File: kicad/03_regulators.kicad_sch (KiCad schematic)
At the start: 20 parts, among them U10 TPS73033DBVT, U3 TPS73033DBVT, U8 K7805-2000R3, U9 VXO7805-500

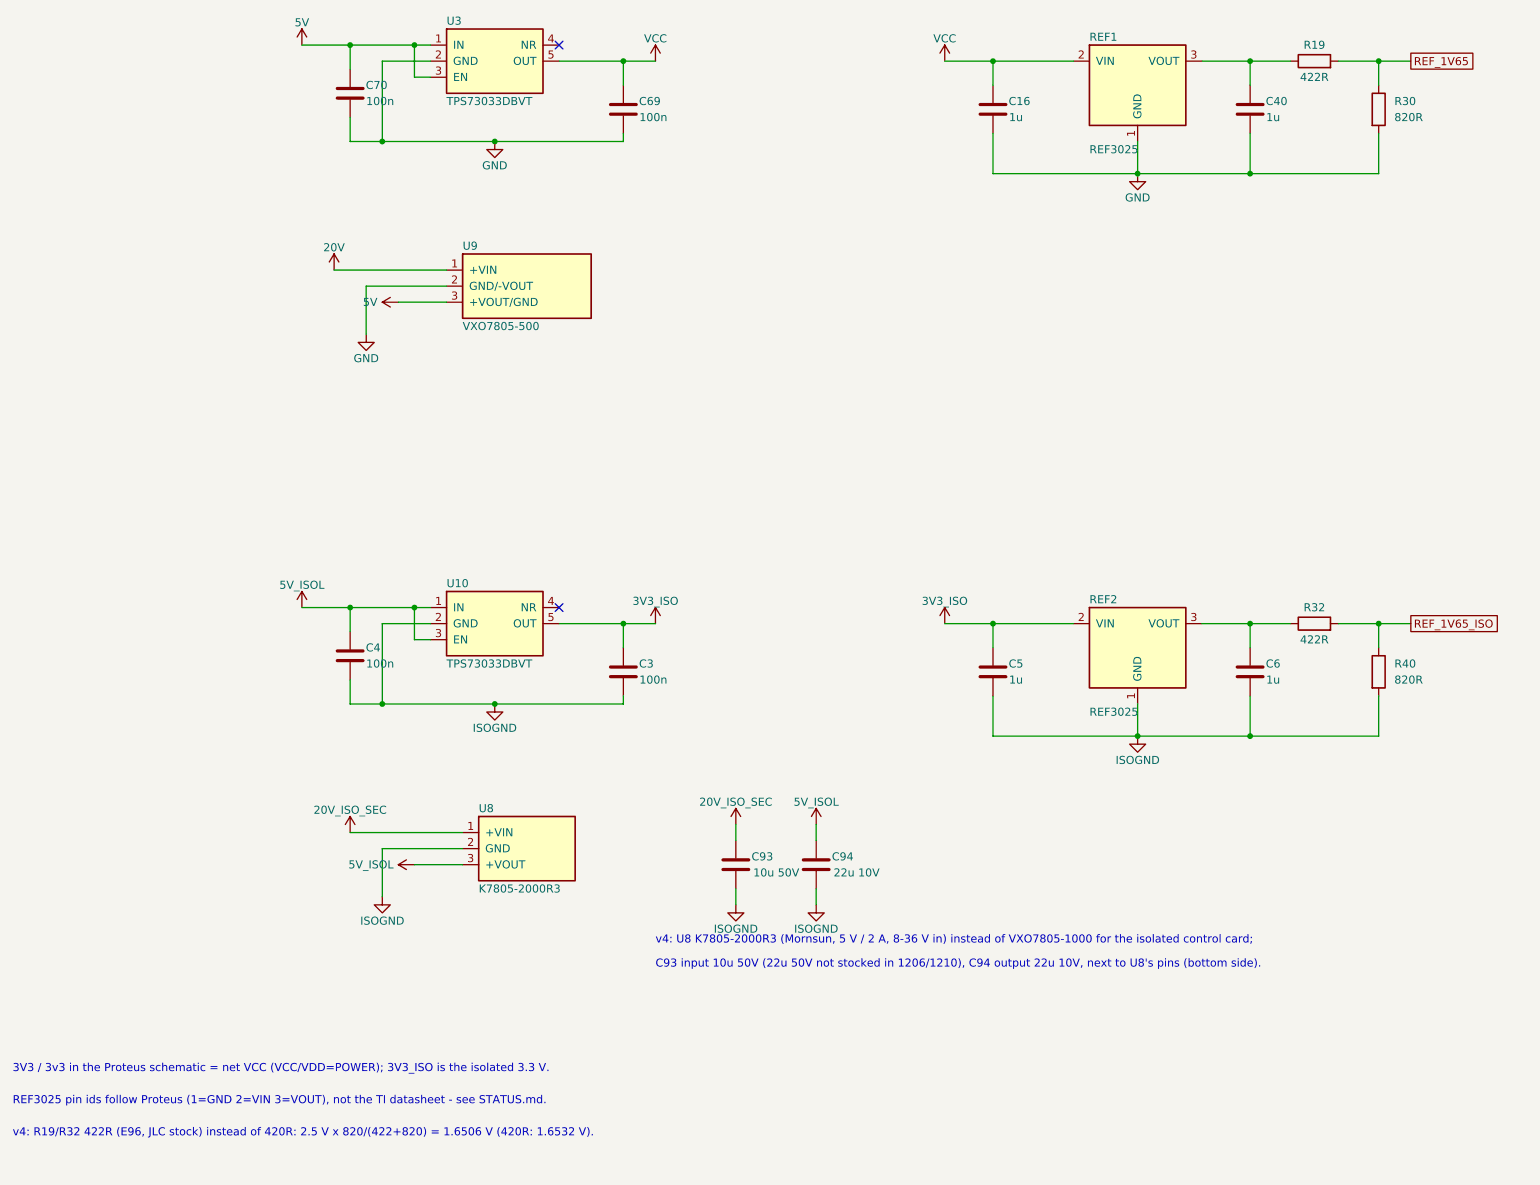
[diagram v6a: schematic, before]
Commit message: v4 fix 11/12: measurement filters (reports/noise findings 1-5), AMC1306M05
Schematic (sheets 1/3/4/5/9): C95-C106 1n C0G across every 10k leg of the six
difference amplifiers (15.9 kHz tap-node filter), R7 1k -> 10k (U1B + leg
matched; ADA3 scaling changes), R18/R9 100R -> 8.2k with C88/C89 4.7n C0G and
new C107/C108 4.7n on ISOADA1/2 (4.1 kHz), C42/C2 1n -> 10n C0G (1.9 kHz DC
links), C109/C110 100n on REF_1V65/REF_1V65_ISO. R64/DAB series R unchanged
(L unknown; 25R per leg for 10 nH).
Board: fix 11 places the 16 caps (10 top beside their resistor, 6 bottom with
7 vias), renames six auto-named output nets, sets the values; fix 12 re-runs
fix 8's silk placement. DRC 293 (+1 silk), 0 shorts/unconnected/parity.
Deviation rows, v4_copper vias/areas, part map. Replay of fixes 1-12 on the
tag's board gives the board and edit log.
fab: C0G codes C307441/C1518204/C22400107, U4-U6 AMC1306M05DWVR (C701717,
+-50 mV, 4.9k R_IND, checked in SBAS734D), CPL 205 parts, stock for 5 boards
(AMC1306M05: 5 in stock). Noise report: CMTI 50 kV/us min correction.

Co-Authored-By: Claude Opus 5.5 <noreply@anthropic.com>
Claude-Session: https://claude.ai/code/session_01Am5hpeWpvZbzmHWspFiWJm
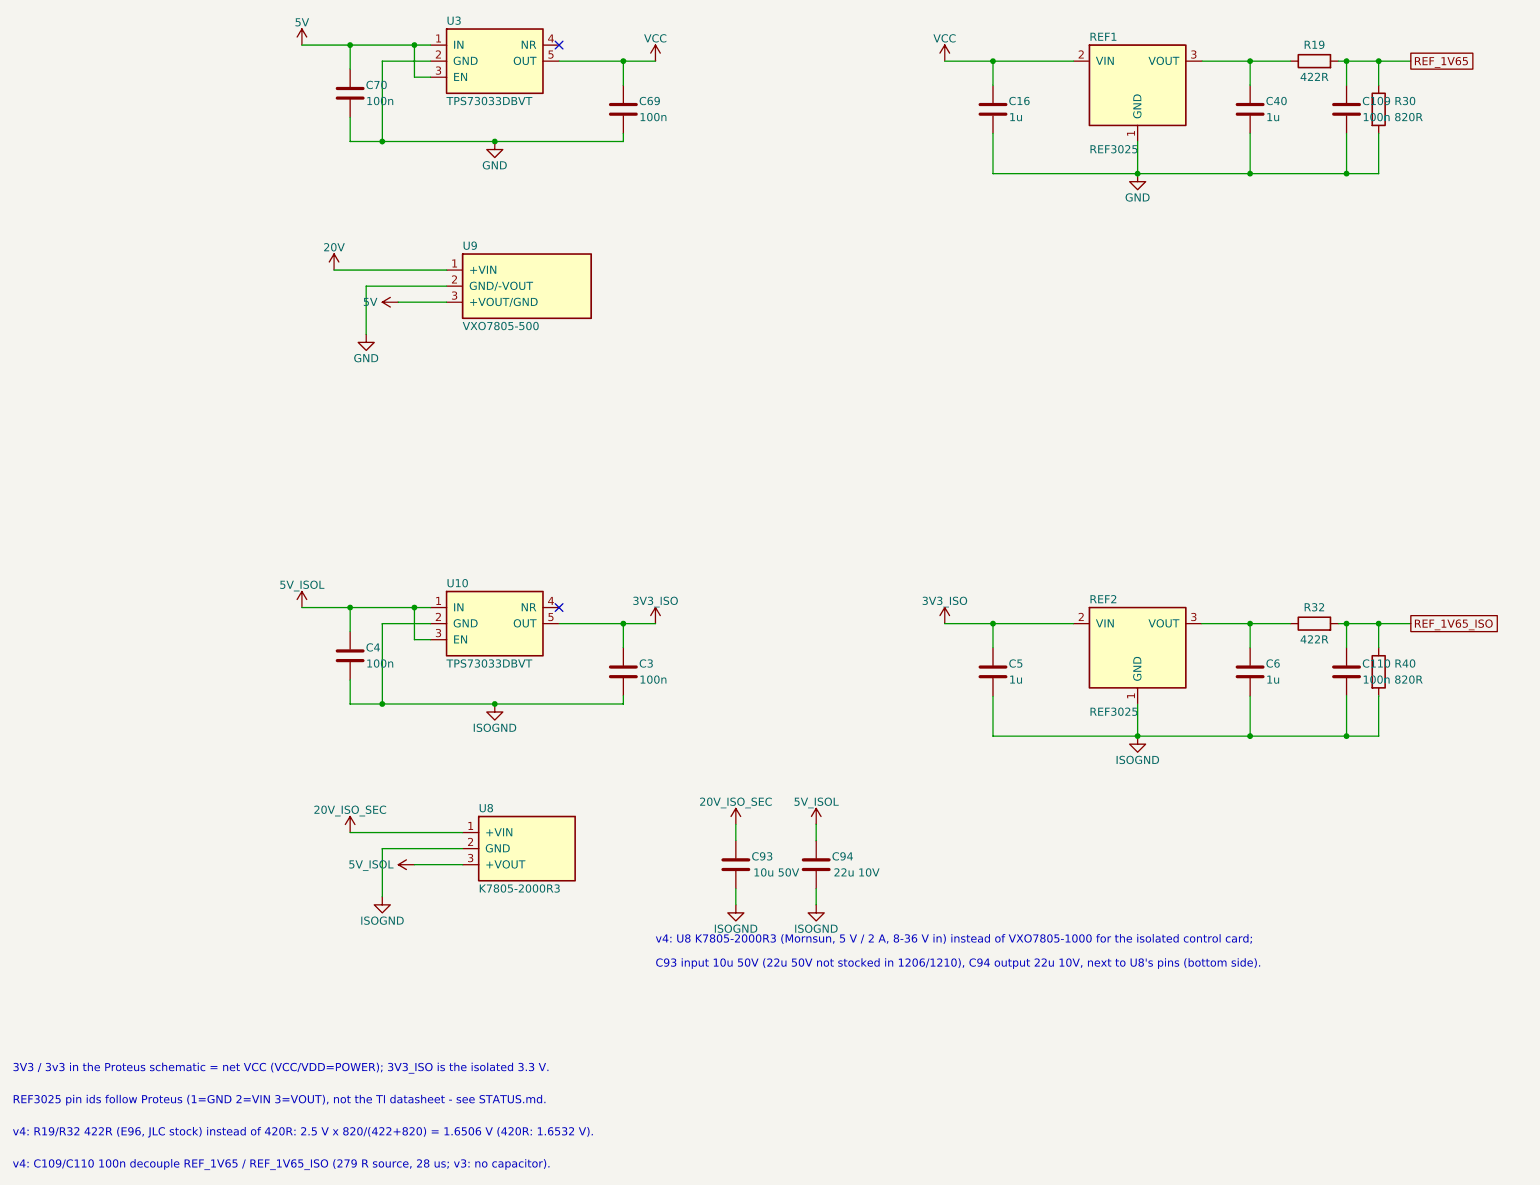
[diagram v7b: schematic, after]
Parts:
- added C109, C110: 100n, Capacitor_SMD:C_0402_1005Metric, symbol ac_psu:C
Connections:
- net GND: now also C109.2
- net ISOGND: now also C110.2
- net REF_1V65: now also C109.1
- net REF_1V65_ISO: now also C110.1
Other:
- note added: "v4: C109/C110 100n decouple REF_1V65 / REF_1V65_ISO (279 R source, 28 us; v3: no capacitor)."
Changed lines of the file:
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@@
+	)
+	(symbol
+		(lib_id "ac_psu:C")
+		(at 236.22 58.42 0)
+		(unit 1)
+		(exclude_from_sim no)
+		(in_bom yes)
+		(on_board yes)
+		(dnp no)
+		(property "Reference" "C109"
+			(at 240.96 57.15 0)
+			(effects
+				(font
+					(size 1.27 1.27)
+				)
+			)
+		)
+		(property "Value" "100n"
+			(at 240.96 59.69 0)
+			(effects
+				(font
+					(size 1.27 1.27)
+				)
+			)
+		)
+		(property "Footprint" "Capacitor_SMD:C_0402_1005Metric"
+			(at 237.1852 62.23 0)
+			(effects
+				(font
+					(size 1.27 1.27)
+				)
+				(hide yes)
+			)
+		)
+		(property "Datasheet" ""
+			(at 236.22 58.42 0)
+			(effects
+				(font
+					(size 1.27 1.27)
+				)
+				(hide yes)
+			)
+		)
+		(property "Description" "Unpolarized capacitor"
+			(at 236.22 58.42 0)
+			(effects
+				(font
+					(size 1.27 1.27)
+				)
+				(hide yes)
+			)
+		)
+		(pin "1"
+		)
+		(pin "2"
+		)
+		(instances
+			(project "ac_psu"
+				(path "/04fb09b4-531d-41de-805c-3ed4ed6dcfa8/25c5ca54-388f-4b9c-876e-19a6fbb99a35"
+					(reference "C109")
+					(unit 1)
+				)
+			)
+		)
+	)
+	(wire
+		(pts
+			(xy 236.22 54.61) (xy 236.22 50.8)
+		)
+		(stroke
+			(width 0)
+			(type default)
+		)
+	)
+	(junction
+		(at 236.22 50.8)
+		(diameter 0)
+		(color 0 0 0 0)
+	)
+	(wire
+		(pts
+			(xy 236.22 62.23) (xy 236.22 68.58)
+		)
+		(stroke
+			(width 0)
+			(type default)
+		)
+	)
+	(junction
+		(at 236.22 68.58)
+		(diameter 0)
+		(color 0 0 0 0)
 	)
 	(symbol
@@
 		(color 0 0 0 0)
 	)
+	(symbol
+		(lib_id "ac_psu:C")
+		(at 236.22 147.32 0)
+		(unit 1)
+		(exclude_from_sim no)
+		(in_bom yes)
+		(on_board yes)
+		(dnp no)
+		(property "Reference" "C110"
+			(at 240.96 146.05 0)
+			(effects
+				(font
+					(size 1.27 1.27)
+				)
+			)
+		)
+		(property "Value" "100n"
+			(at 240.96 148.59 0)
+			(effects
+				(font
+					(size 1.27 1.27)
+				)
+			)
+		)
+		(property "Footprint" "Capacitor_SMD:C_0402_1005Metric"
+			(at 237.1852 151.13 0)
+			(effects
+				(font
+					(size 1.27 1.27)
+				)
+				(hide yes)
+			)
+		)
+		(property "Datasheet" ""
+			(at 236.22 147.32 0)
+			(effects
+				(font
+					(size 1.27 1.27)
+				)
+				(hide yes)
+			)
+		)
+		(property "Description" "Unpolarized capacitor"
+			(at 236.22 147.32 0)
+			(effects
+				(font
+					(size 1.27 1.27)
+				)
+				(hide yes)
+			)
+		)
+		(pin "1"
+		)
+		(pin "2"
+		)
+		(instances
+			(project "ac_psu"
+				(path "/04fb09b4-531d-41de-805c-3ed4ed6dcfa8/25c5ca54-388f-4b9c-876e-19a6fbb99a35"
+					(reference "C110")
+					(unit 1)
+				)
+			)
+		)
+	)
+	(wire
+		(pts
+			(xy 236.22 143.51) (xy 236.22 139.7)
+		)
+		(stroke
+			(width 0)
+			(type default)
+		)
+	)
+	(junction
+		(at 236.22 139.7)
+		(diameter 0)
+		(color 0 0 0 0)
+	)
+	(wire
+		(pts
+			(xy 236.22 151.13) (xy 236.22 157.48)
+		)
+		(stroke
+			(width 0)
+			(type default)
+		)
+	)
+	(junction
+		(at 236.22 157.48)
+		(diameter 0)
+		(color 0 0 0 0)
+	)
 	(text "3V3 / 3v3 in the Proteus schematic = net VCC (VCC/VDD=POWER); 3V3_ISO is the isolated 3.3 V."
 		(exclude_from_sim no)
@@
 		(effects
 			(font
+				(size 1.27 1.27)
+			)
+			(justify left bottom)
+		)
+	)
+	(text "v4: C109/C110 100n decouple REF_1V65 / REF_1V65_ISO (279 R source, 28 us; v3: no capacitor)."
+		(exclude_from_sim no)
+		(at 25.4 226.06 0)
+		(effects
+			(font
